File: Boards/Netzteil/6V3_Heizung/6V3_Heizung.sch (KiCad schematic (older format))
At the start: 36 parts, among them P1 6V3_AC, P2 12V_DC, P3 6V3_DC_1, P4 6V3_DC_2, Q3 IRF540N, Q4 IRF540N, U1 TL072

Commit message: Updated Layout
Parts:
- U1: symbol TL072 -> TL072-RESCUE-6V3_Heizung
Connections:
- net labels added: Reference
- net labels removed: Ref
- wire segments 53 -> 56
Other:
- moved on the sheet: Q3, Q4

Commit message: Work in Progress
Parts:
- D5: symbol ZENER -> ZENER-RESCUE-6V3_Heizung
- Q3, Q4: symbol IRF540N -> IRF540N-RESCUE-6V3_Heizung
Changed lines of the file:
@@
 $EndComp
 $Comp
-L ZENER D5
+L ZENER-RESCUE-6V3_Heizung D5
 U 1 1 55C58252
 P 2850 2850
@@
 	7000 3250 7000 3350
 $Comp
-L IRF540N Q3
+L IRF540N-RESCUE-6V3_Heizung Q3
 U 1 1 55C6C398
 P 5500 4900
@@
 	5600 4300 5600 4700
 $Comp
-L IRF540N Q4
+L IRF540N-RESCUE-6V3_Heizung Q4
 U 1 1 55C6E7F4
 P 5600 2700

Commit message: Work in Progress
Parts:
- C1, C13, C14, C15, C16, C2, C5, C6, C7, C8, C9: symbol C -> Device:C
- C10, C11, C12, C3: symbol CP -> Device:CP
- D1, D2, D3, D4: symbol D_Schottky -> Device:D_Schottky
- D5: symbol ZENER-RESCUE-6V3_Heizung -> 6V3_Heizung-rescue:ZENER-RESCUE-6V3_Heizung
- P1, P3, P4: symbol CONN_2 -> borniers:CONN_2
- P2: footprint MiniUniversalMate-N-LokSockets_13Aug2012:MiniUniversalMate-N-LokSocket_2PinVertical_12Aug2012 -> Connectors_Molex:Molex_KK-6410-02_02x2.54mm_Straight; symbol CONN_2 -> borniers:CONN_2
- Q3, Q4: symbol IRF540N-RESCUE-6V3_Heizung -> 6V3_Heizung-rescue:IRF540N-RESCUE-6V3_Heizung
- R1, R2, R3, R4, R5, R6, R7, R8, R9: symbol R -> Device:R
- U1: symbol TL072-RESCUE-6V3_Heizung -> 6V3_Heizung-rescue:TL072-RESCUE-6V3_Heizung
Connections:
- wire segments 56 -> 92

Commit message: Converted to Kicad 5.1 and Layout changes
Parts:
- removed Q3, Q4: IRF540N, w_to:to220-horiz_5772, symbol 6V3_Heizung-rescue:IRF540N-RESCUE-6V3_Heizung
- added Q1, Q2: IRF540N, Package_TO_SOT_THT:TO-220-3_Vertical, symbol Transistor_FET:IRF540N
- C1, C13, C14, C15, C16, C2, C5, C6, C7, C8, C9: footprint Capacitors_ThroughHole:C_Disc_D3_P2.5 -> Capacitor_THT:C_Disc_D3.0mm_W2.0mm_P2.50mm
- C10: footprint w_capacitors:CP_35x40mm -> Capacitor_THT:CP_Radial_D35.0mm_P10.00mm_SnapIn
- C11, C12, C3: footprint w_capacitors:CP_10x16mm -> Capacitor_THT:CP_Radial_D10.0mm_P5.00mm
- D1, D2, D3, D4: footprint Diodes_ThroughHole:Diode_TO-220_Vertical -> Package_TO_SOT_THT:TO-220-2_Vertical
- D5: footprint w_to:to92_3_flat -> Package_TO_SOT_THT:TO-92-2
- P1, P3, P4: footprint MiniUniversalMate-N-LokSockets_13Aug2012:MiniUniversalMate-N-LokSocket_2PinVertical_12Aug2012 -> Connector_TE-Connectivity:TE_MATE-N-LOK_1-770866-x_1x02_P4.14mm_Vertical; symbol borniers:CONN_2 -> 6V3_Heizung-rescue:CONN_2-borniers
- P2: footprint Connectors_Molex:Molex_KK-6410-02_02x2.54mm_Straight -> Connector_Molex:Molex_KK-254_AE-6410-02A_1x02_P2.54mm_Vertical; symbol borniers:CONN_2 -> 6V3_Heizung-rescue:CONN_2-borniers
- R1, R2, R3, R4, R5, R6, R7, R8, R9: footprint Resistors_ThroughHole:Resistor_Horizontal_RM10mm -> Resistor_THT:R_Axial_DIN0207_L6.3mm_D2.5mm_P10.16mm_Horizontal
- U1: footprint Sockets_DIP:DIP-8__300 -> Package_DIP:DIP-8_W7.62mm

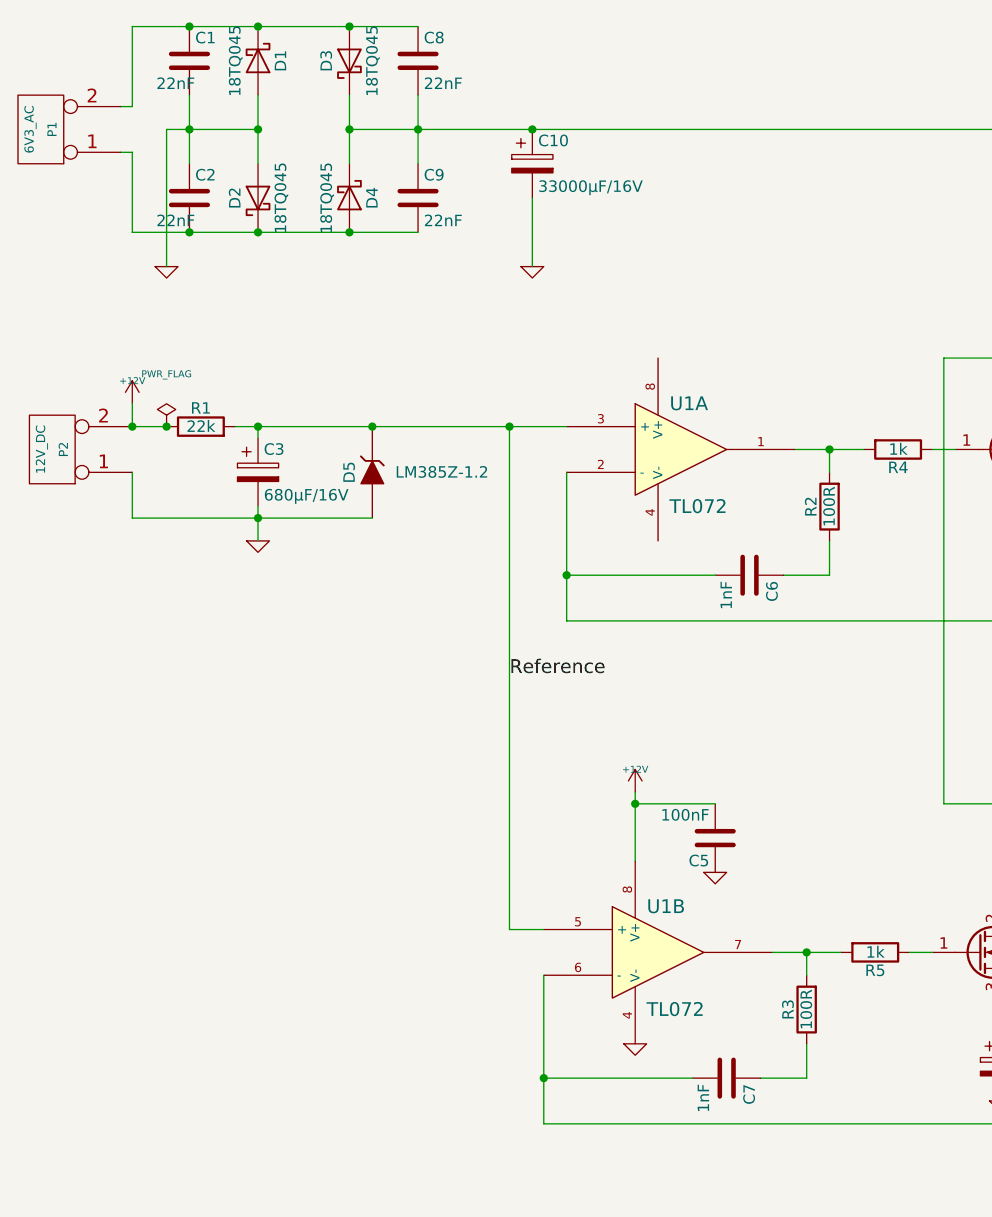
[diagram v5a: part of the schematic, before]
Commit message: Layout changes, Supply connector changes, Mounting holes
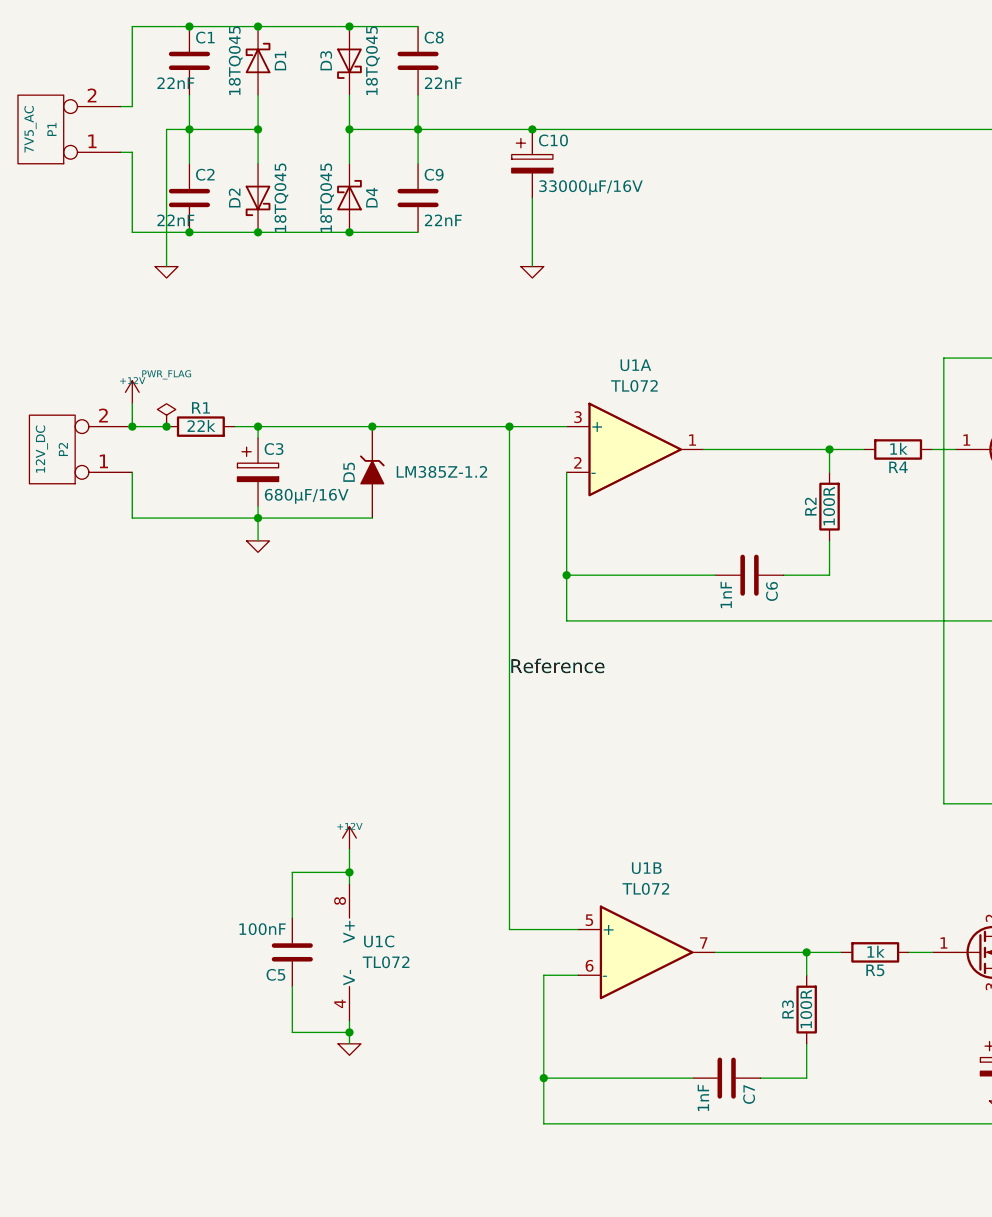
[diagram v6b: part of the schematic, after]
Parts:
- removed U1: TL072, Package_DIP:DIP-8_W7.62mm, symbol 6V3_Heizung-rescue:TL072-RESCUE-6V3_Heizung
- added U1: TL072, Package_DIP:DIP-8_W7.62mm, symbol Amplifier_Operational:TL072
- C10: footprint Capacitor_THT:CP_Radial_D35.0mm_P10.00mm_SnapIn -> Capacitor_THT:CP_Radial_D18.0mm_P7.50mm
- P1: value 6V3_AC -> 7V5_AC
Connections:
- net +12V: now also U1.8 (V+)
- net GND: now also U1.4 (V-)
- net Reference: now also U1.3 (+), U1.5 (+)
- net at R3.2, R5.2: now also U1.7
- net at C14.1, C7.2, R8.1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: now also U1.6 (-)
- net at R2.2, R4.2: now also U1.1
- net at C13.1, C6.2, R6.1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: now also U1.2 (-)
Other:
- moved on the sheet: C5
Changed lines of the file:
@@
 P 1400 1350
 F 0 "P1" V 1350 1350 40  0000 C CNN
-F 1 "6V3_AC" V 1450 1350 40  0000 C CNN
+F 1 "7V5_AC" V 1450 1350 40  0000 C CNN
 F 2 "Connector_TE-Connectivity:TE_MATE-N-LOK_1-770866-x_1x02_P4.14mm_Vertical" H 1400 1350 60  0001 C CNN
 F 3 "" H 1400 1350 60  0000 C CNN
@@
 F 0 "C10" H 3575 1600 50  0000 L CNN
 F 1 "33000µF/16V" H 3575 1400 50  0000 L CNN
-F 2 "Capacitor_THT:CP_Radial_D35.0mm_P10.00mm_SnapIn" H 3588 1350 30  0001 C CNN
+F 2 "Capacitor_THT:CP_Radial_D18.0mm_P7.50mm" H 3588 1350 30  0001 C CNN
 F 3 "" H 3550 1500 60  0000 C CNN
 	1    3550 1500
@@
 L power:+12V #PWR03
 U 1 1 55B6FB5D
-P 4000 4250
-F 0 "#PWR03" H 4000 4200 20  0001 C CNN
-F 1 "+12V" H 4000 4350 30  0000 C CNN
-F 2 "" H 4000 4250 60  0000 C CNN
-F 3 "" H 4000 4250 60  0000 C CNN
-	1    4000 4250
-	1    0    0    -1
-$EndComp
-$Comp
-L 6V3_Heizung-rescue:GND-RESCUE-6V3_Heizung #PWR04
-U 1 1 55B6FB63
-P 4000 5350
-F 0 "#PWR04" H 4000 5350 30  0001 C CNN
-F 1 "GND" H 4000 5280 30  0001 C CNN
-F 2 "" H 4000 5350 60  0000 C CNN
-F 3 "" H 4000 5350 60  0000 C CNN
-	1    4000 5350
+P 2750 4500
+F 0 "#PWR03" H 2750 4450 20  0001 C CNN
+F 1 "+12V" H 2750 4600 30  0000 C CNN
+F 2 "" H 2750 4500 60  0000 C CNN
+F 3 "" H 2750 4500 60  0000 C CNN
+	1    2750 4500
 	1    0    0    -1
 $EndComp
@@
 	1    0    0    -1
 $EndComp
-$Comp
-L Device:C C5
-U 1 1 55B6FB87
-P 4350 4450
-F 0 "C5" H 4375 4550 50  0000 L CNN
-F 1 "100nF" H 4375 4350 50  0000 L CNN
-F 2 "Capacitor_THT:C_Disc_D3.0mm_W2.0mm_P2.50mm" H 4388 4300 30  0001 C CNN
-F 3 "" H 4350 4450 60  0000 C CNN
-	1    4350 4450
-	-1   0    0    1
-$EndComp
-Wire Wire Line
-	4600 4950 4750 4950
 Wire Wire Line
 	4750 5050 4750 4950
@@
 Wire Wire Line
 	4250 5500 3600 5500
-Wire Wire Line
-	4000 4250 4000 4300
-Wire Wire Line
-	4350 4300 4000 4300
-Connection ~ 4000 4300
-$Comp
-L 6V3_Heizung-rescue:GND-RESCUE-6V3_Heizung #PWR05
-U 1 1 55B6FB97
-P 4350 4600
-F 0 "#PWR05" H 4350 4600 30  0001 C CNN
-F 1 "GND" H 4350 4530 30  0001 C CNN
-F 2 "" H 4350 4600 60  0000 C CNN
-F 3 "" H 4350 4600 60  0000 C CNN
-	1    4350 4600
-	1    0    0    -1
-$EndComp
 $Comp
 L 6V3_Heizung-rescue:GND-RESCUE-6V3_Heizung #PWR06
@@
 Connection ~ 1800 2650
 Wire Wire Line
-	3450 4850 3600 4850
-Wire Wire Line
 	1800 2650 1950 2650
 Wire Wire Line
@@
 $EndComp
 Wire Wire Line
-	4700 2750 4850 2750
-Wire Wire Line
 	4850 2850 4850 2750
 Connection ~ 4850 2750
@@
 	5700 1350 5700 2350
 $Comp
-L 6V3_Heizung-rescue:TL072-RESCUE-6V3_Heizung U1
-U 2 1 55C699E6
-P 4100 4950
-F 0 "U1" H 4050 5150 60  0000 L CNN
-F 1 "TL072" H 4050 4700 60  0000 L CNN
-F 2 "Package_DIP:DIP-8_W7.62mm" H 4100 4950 60  0001 C CNN
-F 3 "" H 4100 4950 60  0000 C CNN
-	2    4100 4950
-	1    0    0    -1
-$EndComp
-$Comp
-L 6V3_Heizung-rescue:TL072-RESCUE-6V3_Heizung U1
-U 1 1 55C69AE5
-P 4200 2750
-F 0 "U1" H 4150 2950 60  0000 L CNN
-F 1 "TL072" H 4150 2500 60  0000 L CNN
-F 2 "Package_DIP:DIP-8_W7.62mm" H 4200 2750 60  0001 C CNN
-F 3 "" H 4200 2750 60  0000 C CNN
-	1    4200 2750
-	1    0    0    -1
-$EndComp
-$Comp
 L power:PWR_FLAG #FLG016
 U 1 1 55CD44FA
@@
 	4750 4950 4900 4950
 Wire Wire Line
-	4000 4300 4000 4550
-Wire Wire Line
 	3600 5500 3600 5700
 Wire Wire Line
@@
 	5700 2950 5700 3050
 Connection ~ 5700 3050
+$Comp
+L Device:C C5
+U 1 1 55B6FB87
+P 2500 4950
+F 0 "C5" H 2525 5050 50  0000 L CNN
+F 1 "100nF" H 2525 4850 50  0000 L CNN
+F 2 "Capacitor_THT:C_Disc_D3.0mm_W2.0mm_P2.50mm" H 2538 4800 30  0001 C CNN
+F 3 "" H 2500 4950 60  0000 C CNN
+	1    2500 4950
+	-1   0    0    1
+$EndComp
+$Comp
+L 6V3_Heizung-rescue:GND-RESCUE-6V3_Heizung #PWR0101
+U 1 1 5DA809B9
+P 2750 5350
+F 0 "#PWR0101" H 2750 5350 30  0001 C CNN
+F 1 "GND" H 2750 5280 30  0001 C CNN
+F 2 "" H 2750 5350 60  0000 C CNN
+F 3 "" H 2750 5350 60  0000 C CNN
+	1    2750 5350
+	1    0    0    -1
+$EndComp
+$Comp
+L Amplifier_Operational:TL072 U1
+U 1 1 5DA97C8C
+P 4000 2750
+F 0 "U1" H 4000 3117 50  0000 C CNN
+F 1 "TL072" H 4000 3026 50  0000 C CNN
+F 2 "Package_DIP:DIP-8_W7.62mm" H 4000 2750 50  0001 C CNN
+F 3 "http://www.ti.com/lit/ds/symlink/tl071.pdf" H 4000 2750 50  0001 C CNN
+	1    4000 2750
+	1    0    0    -1
+$EndComp
+$Comp
+L Amplifier_Operational:TL072 U1
+U 2 1 5DA9C773
+P 4050 4950
+F 0 "U1" H 4050 5317 50  0000 C CNN
+F 1 "TL072" H 4050 5226 50  0000 C CNN
+F 2 "Package_DIP:DIP-8_W7.62mm" H 4050 4950 50  0001 C CNN
+F 3 "http://www.ti.com/lit/ds/symlink/tl071.pdf" H 4050 4950 50  0001 C CNN
+	2    4050 4950
+	1    0    0    -1
+$EndComp
+$Comp
+L Amplifier_Operational:TL072 U1
+U 3 1 5DA9FE4C
+P 2850 4950
+F 0 "U1" H 2808 4996 50  0000 L CNN
+F 1 "TL072" H 2808 4905 50  0000 L CNN
+F 2 "Package_DIP:DIP-8_W7.62mm" H 2850 4950 50  0001 C CNN
+F 3 "http://www.ti.com/lit/ds/symlink/tl071.pdf" H 2850 4950 50  0001 C CNN
+	3    2850 4950
+	1    0    0    -1
+$EndComp
+Wire Wire Line
+	2750 4650 2750 4600
+Wire Wire Line
+	2750 5350 2750 5300
+Wire Wire Line
+	2500 4800 2500 4600
+Wire Wire Line
+	2500 4600 2750 4600
+Connection ~ 2750 4600
+Wire Wire Line
+	2750 4600 2750 4500
+Wire Wire Line
+	2500 5100 2500 5300
+Wire Wire Line
+	2500 5300 2750 5300
+Connection ~ 2750 5300
+Wire Wire Line
+	2750 5300 2750 5250
+Wire Wire Line
+	3750 5050 3600 5050
+Wire Wire Line
+	3450 4850 3750 4850
+Wire Wire Line
+	4350 4950 4750 4950
+Wire Wire Line
+	4300 2750 4850 2750
 $EndSCHEMATC
